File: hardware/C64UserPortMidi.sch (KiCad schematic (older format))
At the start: 12 parts, among them J1 C64-UserPort, J2 MIDI IN DIN-5, J3 AVR-ISP-6, U1 ATtiny13A-PU, U2 6N138, U3 74HC595

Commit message: First version of hardware pcb design completed.
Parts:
- C1, C2: footprint (none) -> Capacitor_THT:CP_Radial_D5.0mm_P2.00mm
- J1: footprint Hackup_Commodore:C64-User-Port-Female -> Commodore64C:Connector_Edge_2x12_P3.96mm
- J2: footprint (none) -> Video Connectors:din-5
- J3: footprint (none) -> Connector_PinHeader_2.54mm:PinHeader_2x03_P2.54mm_Vertical
- R1, R2, R3: footprint (none) -> Resistor_THT:R_Axial_DIN0207_L6.3mm_D2.5mm_P7.62mm_Horizontal
- U1: footprint Package_DIP:DIP-8_W7.62mm -> Package_DIP:DIP-8_W7.62mm_Socket_LongPads
- U2: footprint (none) -> Package_DIP:DIP-8_W7.62mm_Socket_LongPads
- U3: footprint (none) -> Package_DIP:DIP-16_W7.62mm_Socket_LongPads
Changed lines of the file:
@@
 F 0 "J1" H 9000 4147 60  0000 C CNN
 F 1 "C64-UserPort" H 9000 4041 60  0000 C CNN
-F 2 "Hackup_Commodore:C64-User-Port-Female" H 9000 4050 60  0001 C CNN
+F 2 "Commodore64C:Connector_Edge_2x12_P3.96mm" H 9000 4050 60  0001 C CNN
 F 3 "~" H 9000 2150 60  0001 C CNN
 	1    9000 3000
@@
 F 0 "U1" H 1971 5996 50  0000 R CNN
 F 1 "ATtiny13A-PU" H 1971 5905 50  0000 R CNN
-F 2 "Package_DIP:DIP-8_W7.62mm" H 2500 5950 50  0001 C CIN
+F 2 "Package_DIP:DIP-8_W7.62mm_Socket_LongPads" H 2500 5950 50  0001 C CIN
 F 3 "http://ww1.microchip.com/downloads/en/DeviceDoc/doc8126.pdf" H 2500 5950 50  0001 C CNN
 	1    2500 5950
@@
 F 0 "U2" H 3200 2767 50  0000 C CNN
 F 1 "6N138" H 3200 2676 50  0000 C CNN
-F 2 "" H 3490 2000 50  0001 C CNN
+F 2 "Package_DIP:DIP-8_W7.62mm_Socket_LongPads" H 3490 2000 50  0001 C CNN
 F 3 "http://www.onsemi.com/pub/Collateral/HCPL2731-D.pdf" H 3490 2000 50  0001 C CNN
 	1    3200 2300
@@
 F 0 "U3" H 6050 3450 50  0000 C CNN
 F 1 "74HC595" H 6050 3350 50  0000 C CNN
-F 2 "" H 6300 2700 50  0001 C CNN
+F 2 "Package_DIP:DIP-16_W7.62mm_Socket_LongPads" H 6300 2700 50  0001 C CNN
 F 3 "http://www.ti.com/lit/ds/symlink/sn74hc595.pdf" H 6300 2700 50  0001 C CNN
 	1    6300 2700
@@
 $EndComp
 $Comp
-L power:GND #PWR?
+L power:GND #PWR0101
 U 1 1 6037C21D
 P 8500 3200
-F 0 "#PWR?" H 8500 2950 50  0001 C CNN
+F 0 "#PWR0101" H 8500 2950 50  0001 C CNN
 F 1 "GND" V 8505 3072 50  0000 R CNN
 F 2 "" H 8500 3200 50  0001 C CNN
@@
 $EndComp
 $Comp
-L power:GND #PWR?
+L power:GND #PWR0102
 U 1 1 6037C5F9
 P 9500 3200
-F 0 "#PWR?" H 9500 2950 50  0001 C CNN
+F 0 "#PWR0102" H 9500 2950 50  0001 C CNN
 F 1 "GND" V 9505 3072 50  0000 R CNN
 F 2 "" H 9500 3200 50  0001 C CNN
@@
 $EndComp
 $Comp
-L power:GND #PWR?
+L power:GND #PWR0103
 U 1 1 6037CA70
 P 9500 2100
-F 0 "#PWR?" H 9500 1850 50  0001 C CNN
+F 0 "#PWR0103" H 9500 1850 50  0001 C CNN
 F 1 "GND" V 9505 1972 50  0000 R CNN
 F 2 "" H 9500 2100 50  0001 C CNN
@@
 $EndComp
 $Comp
-L power:VCC #PWR?
+L power:VCC #PWR0104
 U 1 1 6037D148
 P 9500 2200
-F 0 "#PWR?" H 9500 2050 50  0001 C CNN
+F 0 "#PWR0104" H 9500 2050 50  0001 C CNN
 F 1 "VCC" V 9515 2328 50  0000 L CNN
 F 2 "" H 9500 2200 50  0001 C CNN
@@
 D1
 $Comp
-L power:GND #PWR?
+L power:GND #PWR0105
 U 1 1 6037BAEE
 P 8150 2100
-F 0 "#PWR?" H 8150 1850 50  0001 C CNN
+F 0 "#PWR0105" H 8150 1850 50  0001 C CNN
 F 1 "GND" V 8155 1972 50  0000 R CNN
 F 2 "" H 8150 2100 50  0001 C CNN
@@
 D7
 $Comp
-L power:VCC #PWR?
+L power:VCC #PWR0106
 U 1 1 603A4E22
 P 6300 2100
-F 0 "#PWR?" H 6300 1950 50  0001 C CNN
+F 0 "#PWR0106" H 6300 1950 50  0001 C CNN
 F 1 "VCC" H 6315 2273 50  0000 C CNN
 F 2 "" H 6300 2100 50  0001 C CNN
@@
 $EndComp
 $Comp
-L power:GND #PWR?
+L power:GND #PWR0107
 U 1 1 603A61EE
 P 6300 3400
-F 0 "#PWR?" H 6300 3150 50  0001 C CNN
+F 0 "#PWR0107" H 6300 3150 50  0001 C CNN
 F 1 "GND" H 6305 3227 50  0000 C CNN
 F 2 "" H 6300 3400 50  0001 C CNN
@@
 F 0 "J2" H 1900 1975 50  0000 C CNN
 F 1 "MIDI IN DIN-5" H 1900 1884 50  0000 C CNN
-F 2 "" H 1900 2250 50  0001 C CNN
+F 2 "Video Connectors:din-5" H 1900 2250 50  0001 C CNN
 F 3 "http://www.mouser.com/ds/2/18/40_c091_abd_e-75918.pdf" H 1900 2250 50  0001 C CNN
 	1    1900 2250
@@
 ATtiny Micro
 $Comp
-L power:GND #PWR?
+L power:GND #PWR0108
 U 1 1 603B1A67
 P 2500 6550
-F 0 "#PWR?" H 2500 6300 50  0001 C CNN
+F 0 "#PWR0108" H 2500 6300 50  0001 C CNN
 F 1 "GND" H 2505 6377 50  0000 C CNN
 F 2 "" H 2500 6550 50  0001 C CNN
@@
 $EndComp
 $Comp
-L power:VCC #PWR?
+L power:VCC #PWR0109
 U 1 1 603B2FD7
 P 2500 5350
-F 0 "#PWR?" H 2500 5200 50  0001 C CNN
+F 0 "#PWR0109" H 2500 5200 50  0001 C CNN
 F 1 "VCC" H 2515 5523 50  0000 C CNN
 F 2 "" H 2500 5350 50  0001 C CNN
@@
 F 0 "R1" V 2657 2150 50  0000 C CNN
 F 1 "220" V 2566 2150 50  0000 C CNN
-F 2 "" V 2380 2150 50  0001 C CNN
+F 2 "Resistor_THT:R_Axial_DIN0207_L6.3mm_D2.5mm_P7.62mm_Horizontal" V 2380 2150 50  0001 C CNN
 F 3 "~" H 2450 2150 50  0001 C CNN
 	1    2450 2150
@@
 F 0 "R2" H 3870 2296 50  0000 L CNN
 F 1 "220" H 3870 2205 50  0000 L CNN
-F 2 "" V 3730 2250 50  0001 C CNN
+F 2 "Resistor_THT:R_Axial_DIN0207_L6.3mm_D2.5mm_P7.62mm_Horizontal" V 3730 2250 50  0001 C CNN
 F 3 "~" H 3800 2250 50  0001 C CNN
 	1    3800 2250
@@
 F 0 "R3" H 3720 2796 50  0000 L CNN
 F 1 "4.7k" H 3720 2705 50  0000 L CNN
-F 2 "" V 3580 2750 50  0001 C CNN
+F 2 "Resistor_THT:R_Axial_DIN0207_L6.3mm_D2.5mm_P7.62mm_Horizontal" V 3580 2750 50  0001 C CNN
 F 3 "~" H 3650 2750 50  0001 C CNN
 	1    3650 2750
@@
 Connection ~ 3800 2100
 $Comp
-L power:VCC #PWR?
+L power:VCC #PWR0110
 U 1 1 603C764D
 P 3800 2000
-F 0 "#PWR?" H 3800 1850 50  0001 C CNN
+F 0 "#PWR0110" H 3800 1850 50  0001 C CNN
 F 1 "VCC" H 3815 2173 50  0000 C CNN
 F 2 "" H 3800 2000 50  0001 C CNN
@@
 	3650 2200 3650 2600
 $Comp
-L power:GND #PWR?
+L power:GND #PWR0111
 U 1 1 603CD880
 P 3650 2900
-F 0 "#PWR?" H 3650 2650 50  0001 C CNN
+F 0 "#PWR0111" H 3650 2650 50  0001 C CNN
 F 1 "GND" H 3655 2727 50  0000 C CNN
 F 2 "" H 3650 2900 50  0001 C CNN
@@
 $EndComp
 $Comp
-L power:GND #PWR?
+L power:GND #PWR0112
 U 1 1 603CEC7E
 P 4000 2650
-F 0 "#PWR?" H 4000 2400 50  0001 C CNN
+F 0 "#PWR0112" H 4000 2400 50  0001 C CNN
 F 1 "GND" H 4005 2477 50  0000 C CNN
 F 2 "" H 4000 2650 50  0001 C CNN
@@
 OE
 $Comp
-L power:VCC #PWR?
+L power:VCC #PWR0113
 U 1 1 603EE609
 P 5800 2800
-F 0 "#PWR?" H 5800 2650 50  0001 C CNN
+F 0 "#PWR0113" H 5800 2650 50  0001 C CNN
 F 1 "VCC" H 5815 2973 50  0000 C CNN
 F 2 "" H 5800 2800 50  0001 C CNN
@@
 F 0 "C2" H 5518 3296 50  0000 L CNN
 F 1 "0.1uF" H 5518 3205 50  0000 L CNN
-F 2 "" H 5438 3100 50  0001 C CNN
+F 2 "Capacitor_THT:CP_Radial_D5.0mm_P2.00mm" H 5438 3100 50  0001 C CNN
 F 3 "~" H 5400 3250 50  0001 C CNN
 	1    5400 3250
@@
 $EndComp
 $Comp
-L power:VCC #PWR?
+L power:VCC #PWR0114
 U 1 1 603F1230
 P 5400 3100
-F 0 "#PWR?" H 5400 2950 50  0001 C CNN
+F 0 "#PWR0114" H 5400 2950 50  0001 C CNN
 F 1 "VCC" H 5415 3273 50  0000 C CNN
 F 2 "" H 5400 3100 50  0001 C CNN
@@
 $EndComp
 $Comp
-L power:GND #PWR?
+L power:GND #PWR0115
 U 1 1 603F18D9
 P 5400 3400
-F 0 "#PWR?" H 5400 3150 50  0001 C CNN
+F 0 "#PWR0115" H 5400 3150 50  0001 C CNN
 F 1 "GND" H 5405 3227 50  0000 C CNN
 F 2 "" H 5400 3400 50  0001 C CNN
@@
 F 0 "J3" H 5021 6146 50  0000 R CNN
 F 1 "AVR-ISP-6" H 5021 6055 50  0000 R CNN
-F 2 "" V 5100 6100 50  0001 C CNN
+F 2 "Connector_PinHeader_2.54mm:PinHeader_2x03_P2.54mm_Vertical" V 5100 6100 50  0001 C CNN
 F 3 " ~" H 4075 5500 50  0001 C CNN
 	1    5350 6050
@@
 FLAG
 $Comp
-L power:VCC #PWR?
+L power:VCC #PWR0116
 U 1 1 60442033
 P 5250 5550
-F 0 "#PWR?" H 5250 5400 50  0001 C CNN
+F 0 "#PWR0116" H 5250 5400 50  0001 C CNN
 F 1 "VCC" H 5265 5723 50  0000 C CNN
 F 2 "" H 5250 5550 50  0001 C CNN
@@
 $EndComp
 $Comp
-L power:GND #PWR?
+L power:GND #PWR0117
 U 1 1 60442485
 P 5250 6450
-F 0 "#PWR?" H 5250 6200 50  0001 C CNN
+F 0 "#PWR0117" H 5250 6200 50  0001 C CNN
 F 1 "GND" H 5255 6277 50  0000 C CNN
 F 2 "" H 5250 6450 50  0001 C CNN
@@
 F 0 "C1" H 3918 5996 50  0000 L CNN
 F 1 "0.1uF" H 3918 5905 50  0000 L CNN
-F 2 "" H 3838 5800 50  0001 C CNN
+F 2 "Capacitor_THT:CP_Radial_D5.0mm_P2.00mm" H 3838 5800 50  0001 C CNN
 F 3 "~" H 3800 5950 50  0001 C CNN
 	1    3800 5950
@@
 $EndComp
 $Comp
-L power:VCC #PWR?
+L power:VCC #PWR0118
 U 1 1 6045AD9D
 P 3800 5800
-F 0 "#PWR?" H 3800 5650 50  0001 C CNN
+F 0 "#PWR0118" H 3800 5650 50  0001 C CNN
 F 1 "VCC" H 3815 5973 50  0000 C CNN
 F 2 "" H 3800 5800 50  0001 C CNN
@@
 $EndComp
 $Comp
-L power:GND #PWR?
+L power:GND #PWR0119
 U 1 1 6045ADA7
 P 3800 6100
-F 0 "#PWR?" H 3800 5850 50  0001 C CNN
+F 0 "#PWR0119" H 3800 5850 50  0001 C CNN
 F 1 "GND" H 3805 5927 50  0000 C CNN
 F 2 "" H 3800 6100 50  0001 C CNN
@@
 $EndComp
 $Comp
-L power:VCC #PWR?
+L power:VCC #PWR0120
 U 1 1 6047CAE1
 P 5700 2600
-F 0 "#PWR?" H 5700 2450 50  0001 C CNN
+F 0 "#PWR0120" H 5700 2450 50  0001 C CNN
 F 1 "VCC" H 5715 2773 50  0000 C CNN
 F 2 "" H 5700 2600 50  0001 C CNN

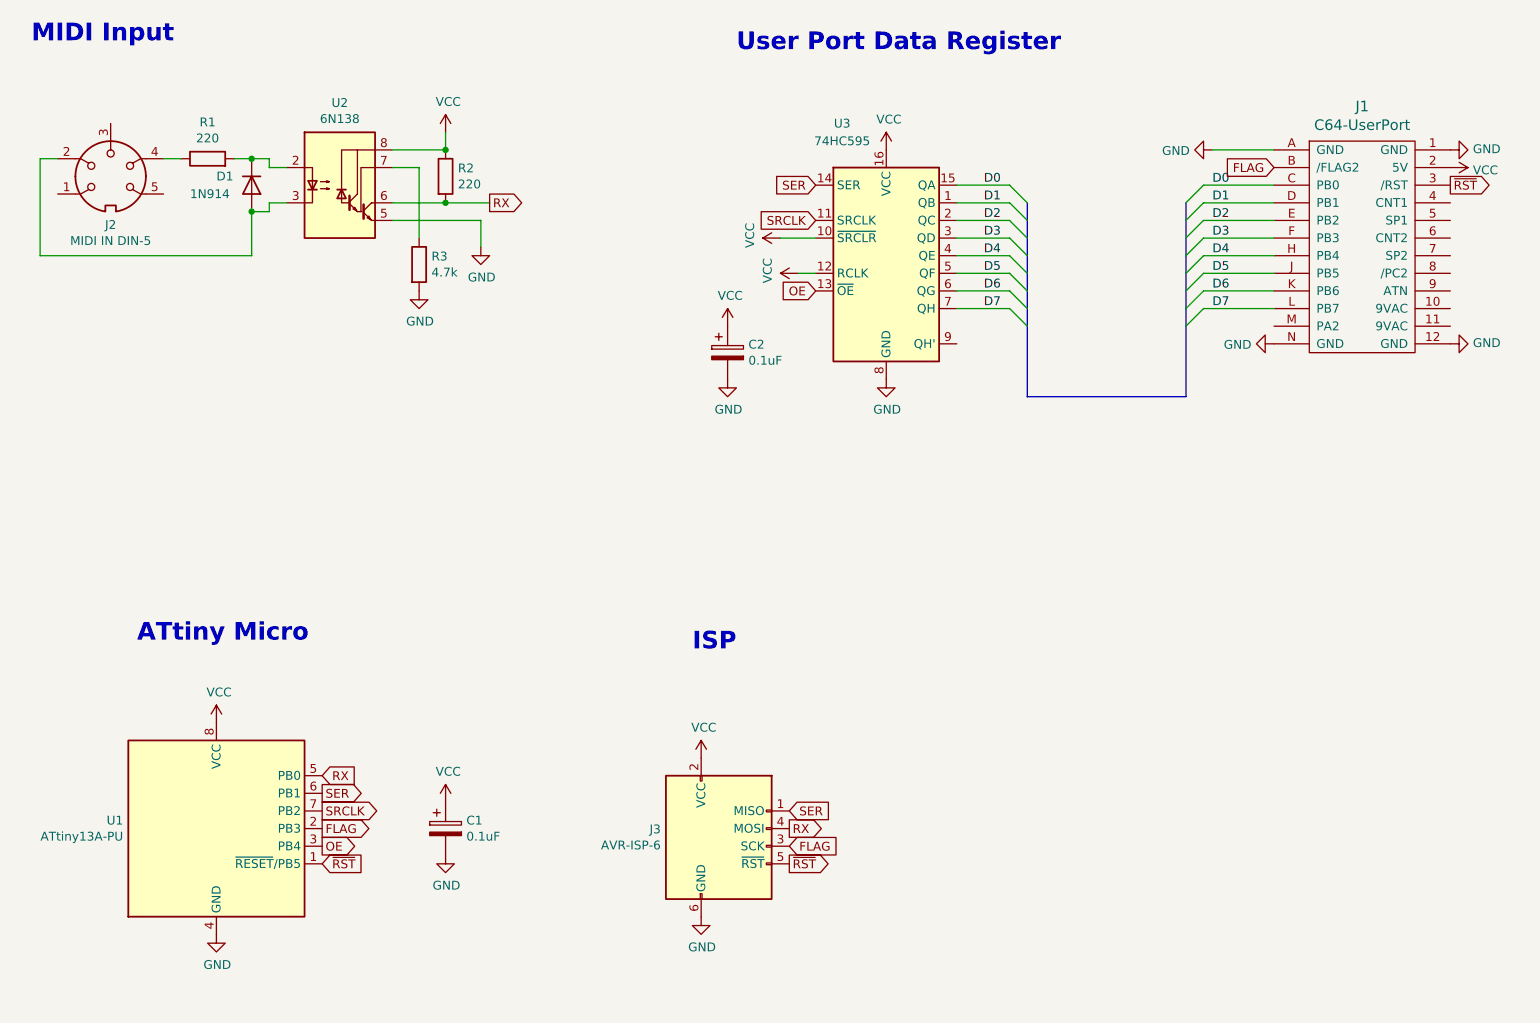
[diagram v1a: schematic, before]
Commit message: Added data led and latch filtering capacitor to hardware design.
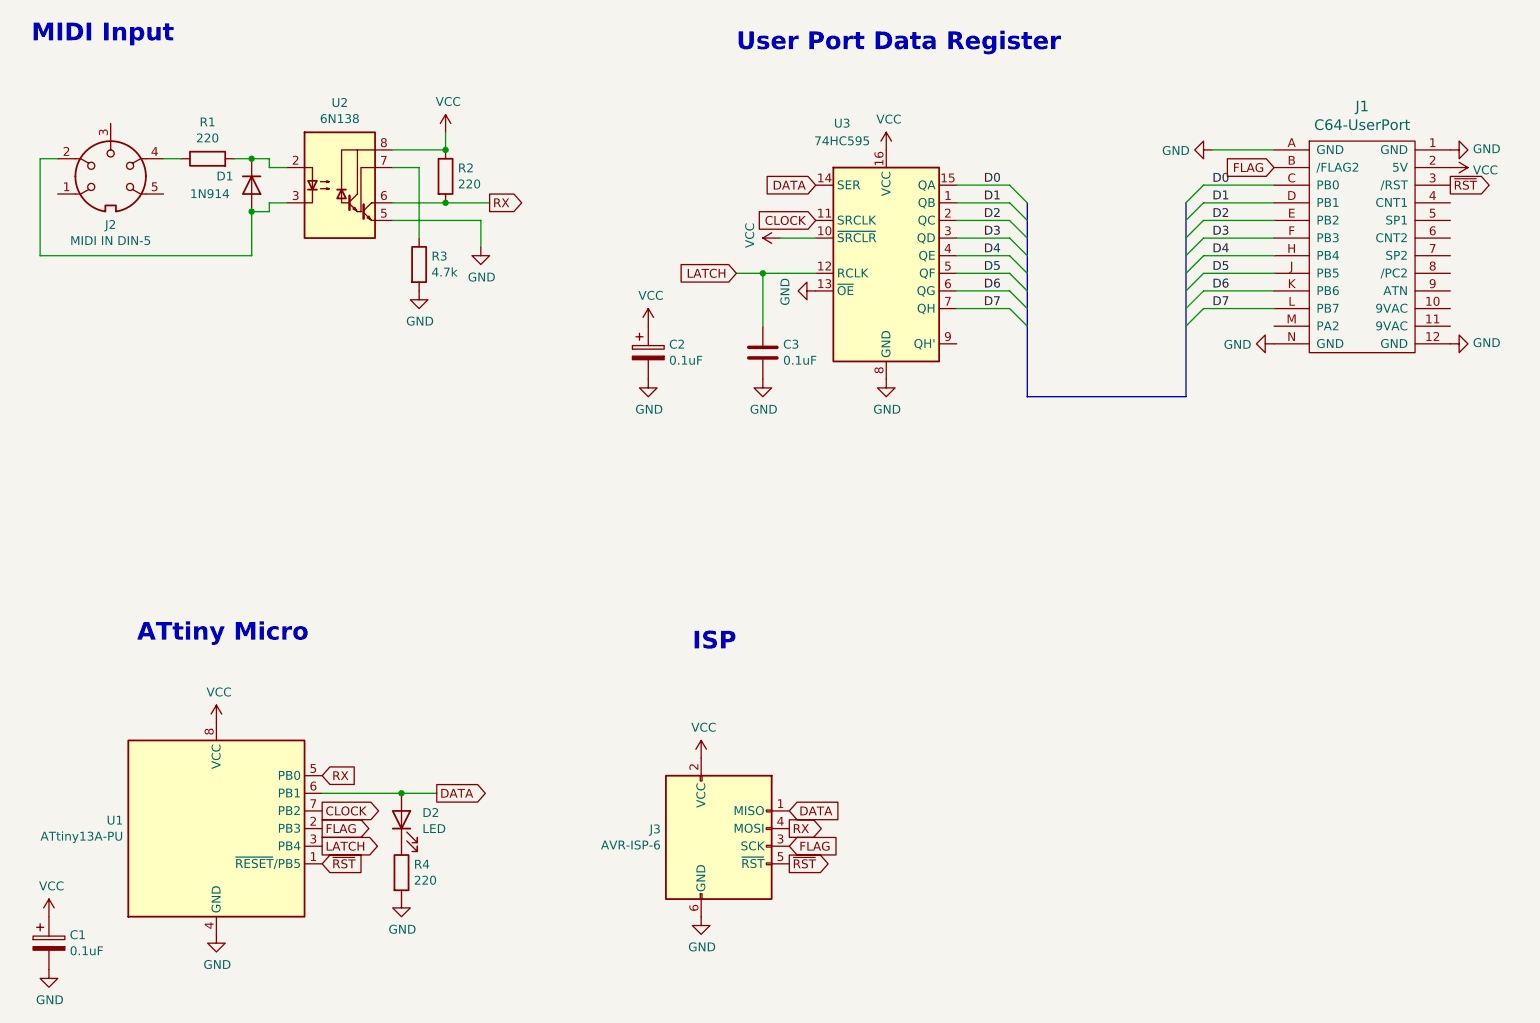
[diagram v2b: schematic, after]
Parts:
- added C3: 0.1uF, Capacitor_THT:C_Disc_D5.0mm_W2.5mm_P2.50mm, symbol Device:C
- added D2: LED, LED_THT:LED_D3.0mm, symbol Device:LED
- added R4: 220, Resistor_THT:R_Axial_DIN0207_L6.3mm_D2.5mm_P7.62mm_Horizontal, symbol Device:R
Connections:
- net GND: now also U3.13 (~OE), C3.2, R4.2
- net VCC: no longer U3.12 (RCLK)
- net OE renamed LATCH
- net LATCH: now also U3.12 (RCLK), C3.1; no longer U3.13 (~OE)
- net SER renamed DATA
- net DATA: now also D2.2 (A)
- net SRCLK renamed CLOCK
- new net: D2.1 (K), R4.1
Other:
- moved on the sheet: C1, C2
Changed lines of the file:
@@
 Text GLabel 3100 5650 2    50   Input ~ 0
 RX
-Text GLabel 3100 5750 2    50   Output ~ 0
-SER
+Text GLabel 3750 5750 2    50   Output ~ 0
+DATA
 Text GLabel 5900 2300 0    50   Input ~ 0
-SER
+DATA
 Text GLabel 5900 2500 0    50   Input ~ 0
-SRCLK
-Text GLabel 5900 2900 0    50   Input ~ 0
-OE
-$Comp
-L power:VCC #PWR0113
-U 1 1 603EE609
-P 5800 2800
-F 0 "#PWR0113" H 5800 2650 50  0001 C CNN
-F 1 "VCC" H 5815 2973 50  0000 C CNN
-F 2 "" H 5800 2800 50  0001 C CNN
-F 3 "" H 5800 2800 50  0001 C CNN
-	1    5800 2800
-	0    -1   -1   0
-$EndComp
+CLOCK
+Text GLabel 5450 2800 0    50   Input ~ 0
+LATCH
 $Comp
 L Device:CP C2
 U 1 1 603EF6AC
-P 5400 3250
-F 0 "C2" H 5518 3296 50  0000 L CNN
-F 1 "0.1uF" H 5518 3205 50  0000 L CNN
-F 2 "Capacitor_THT:CP_Radial_D5.0mm_P2.00mm" H 5438 3100 50  0001 C CNN
-F 3 "~" H 5400 3250 50  0001 C CNN
-	1    5400 3250
+P 4950 3250
+F 0 "C2" H 5068 3296 50  0000 L CNN
+F 1 "0.1uF" H 5068 3205 50  0000 L CNN
+F 2 "Capacitor_THT:CP_Radial_D5.0mm_P2.00mm" H 4988 3100 50  0001 C CNN
+F 3 "~" H 4950 3250 50  0001 C CNN
+	1    4950 3250
 	1    0    0    -1
 $EndComp
@@
 L power:VCC #PWR0114
 U 1 1 603F1230
-P 5400 3100
-F 0 "#PWR0114" H 5400 2950 50  0001 C CNN
-F 1 "VCC" H 5415 3273 50  0000 C CNN
-F 2 "" H 5400 3100 50  0001 C CNN
-F 3 "" H 5400 3100 50  0001 C CNN
-	1    5400 3100
+P 4950 3100
+F 0 "#PWR0114" H 4950 2950 50  0001 C CNN
+F 1 "VCC" H 4965 3273 50  0000 C CNN
+F 2 "" H 4950 3100 50  0001 C CNN
+F 3 "" H 4950 3100 50  0001 C CNN
+	1    4950 3100
 	1    0    0    -1
 $EndComp
@@
 L power:GND #PWR0115
 U 1 1 603F18D9
-P 5400 3400
-F 0 "#PWR0115" H 5400 3150 50  0001 C CNN
-F 1 "GND" H 5405 3227 50  0000 C CNN
-F 2 "" H 5400 3400 50  0001 C CNN
-F 3 "" H 5400 3400 50  0001 C CNN
-	1    5400 3400
+P 4950 3400
+F 0 "#PWR0115" H 4950 3150 50  0001 C CNN
+F 1 "GND" H 4955 3227 50  0000 C CNN
+F 2 "" H 4950 3400 50  0001 C CNN
+F 3 "" H 4950 3400 50  0001 C CNN
+	1    4950 3400
 	1    0    0    -1
 $EndComp
 Text GLabel 8500 2200 0    50   Input ~ 0
 FLAG
-Wire Wire Line
-	5800 2800 5900 2800
 Entry Wire Line
 	7000 2300 7100 2400
@@
 RX
 Text GLabel 5750 5850 2    50   Input ~ 0
-SER
+DATA
 Text GLabel 5750 6050 2    50   Input ~ 0
 FLAG
@@
 L Device:CP C1
 U 1 1 6045AAE5
-P 3800 5950
-F 0 "C1" H 3918 5996 50  0000 L CNN
-F 1 "0.1uF" H 3918 5905 50  0000 L CNN
-F 2 "Capacitor_THT:CP_Radial_D5.0mm_P2.00mm" H 3838 5800 50  0001 C CNN
-F 3 "~" H 3800 5950 50  0001 C CNN
-	1    3800 5950
+P 1550 6600
+F 0 "C1" H 1668 6646 50  0000 L CNN
+F 1 "0.1uF" H 1668 6555 50  0000 L CNN
+F 2 "Capacitor_THT:CP_Radial_D5.0mm_P2.00mm" H 1588 6450 50  0001 C CNN
+F 3 "~" H 1550 6600 50  0001 C CNN
+	1    1550 6600
 	1    0    0    -1
 $EndComp
@@
 L power:VCC #PWR0118
 U 1 1 6045AD9D
-P 3800 5800
-F 0 "#PWR0118" H 3800 5650 50  0001 C CNN
-F 1 "VCC" H 3815 5973 50  0000 C CNN
-F 2 "" H 3800 5800 50  0001 C CNN
-F 3 "" H 3800 5800 50  0001 C CNN
-	1    3800 5800
+P 1550 6450
+F 0 "#PWR0118" H 1550 6300 50  0001 C CNN
+F 1 "VCC" H 1565 6623 50  0000 C CNN
+F 2 "" H 1550 6450 50  0001 C CNN
+F 3 "" H 1550 6450 50  0001 C CNN
+	1    1550 6450
 	1    0    0    -1
 $EndComp
@@
 L power:GND #PWR0119
 U 1 1 6045ADA7
-P 3800 6100
-F 0 "#PWR0119" H 3800 5850 50  0001 C CNN
-F 1 "GND" H 3805 5927 50  0000 C CNN
-F 2 "" H 3800 6100 50  0001 C CNN
-F 3 "" H 3800 6100 50  0001 C CNN
-	1    3800 6100
+P 1550 6750
+F 0 "#PWR0119" H 1550 6500 50  0001 C CNN
+F 1 "GND" H 1555 6577 50  0000 C CNN
+F 2 "" H 1550 6750 50  0001 C CNN
+F 3 "" H 1550 6750 50  0001 C CNN
+	1    1550 6750
 	1    0    0    -1
 $EndComp
@@
 FLAG
 Text GLabel 3100 6050 2    50   Output ~ 0
-OE
+LATCH
 Text GLabel 3100 5850 2    50   Output ~ 0
-SRCLK
+CLOCK
+$Comp
+L Device:C C3
+U 1 1 603F1CF0
+P 5600 3250
+F 0 "C3" H 5715 3296 50  0000 L CNN
+F 1 "0.1uF" H 5715 3205 50  0000 L CNN
+F 2 "Capacitor_THT:C_Disc_D5.0mm_W2.5mm_P2.50mm" H 5638 3100 50  0001 C CNN
+F 3 "~" H 5600 3250 50  0001 C CNN
+	1    5600 3250
+	1    0    0    -1
+$EndComp
+$Comp
+L power:GND #PWR0113
+U 1 1 604056B0
+P 5600 3400
+F 0 "#PWR0113" H 5600 3150 50  0001 C CNN
+F 1 "GND" H 5605 3227 50  0000 C CNN
+F 2 "" H 5600 3400 50  0001 C CNN
+F 3 "" H 5600 3400 50  0001 C CNN
+	1    5600 3400
+	1    0    0    -1
+$EndComp
+$Comp
+L power:GND #PWR0121
+U 1 1 604090CD
+P 5900 2900
+F 0 "#PWR0121" H 5900 2650 50  0001 C CNN
+F 1 "GND" H 5905 2727 50  0000 C CNN
+F 2 "" H 5900 2900 50  0001 C CNN
+F 3 "" H 5900 2900 50  0001 C CNN
+	1    5900 2900
+	0    1    1    0
+$EndComp
+Wire Wire Line
+	5450 2800 5600 2800
+Wire Wire Line
+	5600 2800 5600 3100
+Connection ~ 5600 2800
+Wire Wire Line
+	5600 2800 5900 2800
+$Comp
+L Device:LED D2
+U 1 1 60429892
+P 3550 5900
+F 0 "D2" V 3589 5782 50  0000 R CNN
+F 1 "LED" V 3498 5782 50  0000 R CNN
+F 2 "LED_THT:LED_D3.0mm" H 3550 5900 50  0001 C CNN
+F 3 "~" H 3550 5900 50  0001 C CNN
+	1    3550 5900
+	0    -1   -1   0
+$EndComp
+$Comp
+L Device:R R4
+U 1 1 6042AD7B
+P 3550 6200
+F 0 "R4" H 3620 6246 50  0000 L CNN
+F 1 "220" H 3620 6155 50  0000 L CNN
+F 2 "Resistor_THT:R_Axial_DIN0207_L6.3mm_D2.5mm_P7.62mm_Horizontal" V 3480 6200 50  0001 C CNN
+F 3 "~" H 3550 6200 50  0001 C CNN
+	1    3550 6200
+	1    0    0    -1
+$EndComp
+$Comp
+L power:GND #PWR0122
+U 1 1 60445AF7
+P 3550 6350
+F 0 "#PWR0122" H 3550 6100 50  0001 C CNN
+F 1 "GND" H 3555 6177 50  0000 C CNN
+F 2 "" H 3550 6350 50  0001 C CNN
+F 3 "" H 3550 6350 50  0001 C CNN
+	1    3550 6350
+	1    0    0    -1
+$EndComp
+Wire Wire Line
+	3100 5750 3550 5750
+Wire Wire Line
+	3550 5750 3750 5750
+Connection ~ 3550 5750
 Wire Bus Line
 	8000 2400 8000 3500

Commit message: Fixed pin number mixup from schematic symbol to pcb footprint on midi connector.
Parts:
- removed J2: MIDI IN DIN-5, Video Connectors:din-5, symbol Connector:DIN-5
- added J2: MIDI IN DIN-5, Video Connectors:din-5, symbol hackup-commodore:DIN-5
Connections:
- net at D1.2 (A), U2.3 (C2): now also J2.5
- net at R1.1: now also J2.4
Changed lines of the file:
@@
-	1    0    0    -1
-$EndComp
-$Comp
-L Connector:DIN-5 J2
-U 1 1 603A90E2
-P 1900 2250
-F 0 "J2" H 1900 1975 50  0000 C CNN
-F 1 "MIDI IN DIN-5" H 1900 1884 50  0000 C CNN
-F 2 "Video Connectors:din-5" H 1900 2250 50  0001 C CNN
-F 3 "http://www.mouser.com/ds/2/18/40_c091_abd_e-75918.pdf" H 1900 2250 50  0001 C CNN
-	1    1900 2250
 	1    0    0    -1
 $EndComp
@@
 	3550 5750 3750 5750
 Connection ~ 3550 5750
+$Comp
+L hackup-commodore:DIN-5 J2
+U 1 1 60497A6A
+P 1900 2250
+F 0 "J2" H 1900 1975 50  0000 C CNN
+F 1 "MIDI IN DIN-5" H 1900 1884 50  0000 C CNN
+F 2 "Video Connectors:din-5" H 1900 2250 50  0001 C CNN
+F 3 "http://www.mouser.com/ds/2/18/40_c091_abd_e-75918.pdf" H 1900 2250 50  0001 C CNN
+	1    1900 2250
+	1    0    0    -1
+$EndComp
 Wire Bus Line
 	8000 2400 8000 3500
